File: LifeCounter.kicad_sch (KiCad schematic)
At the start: 17 parts, among them IC1 STM32H562RGT6, IC2 AP3012KTR-E1, J1 54104-4531

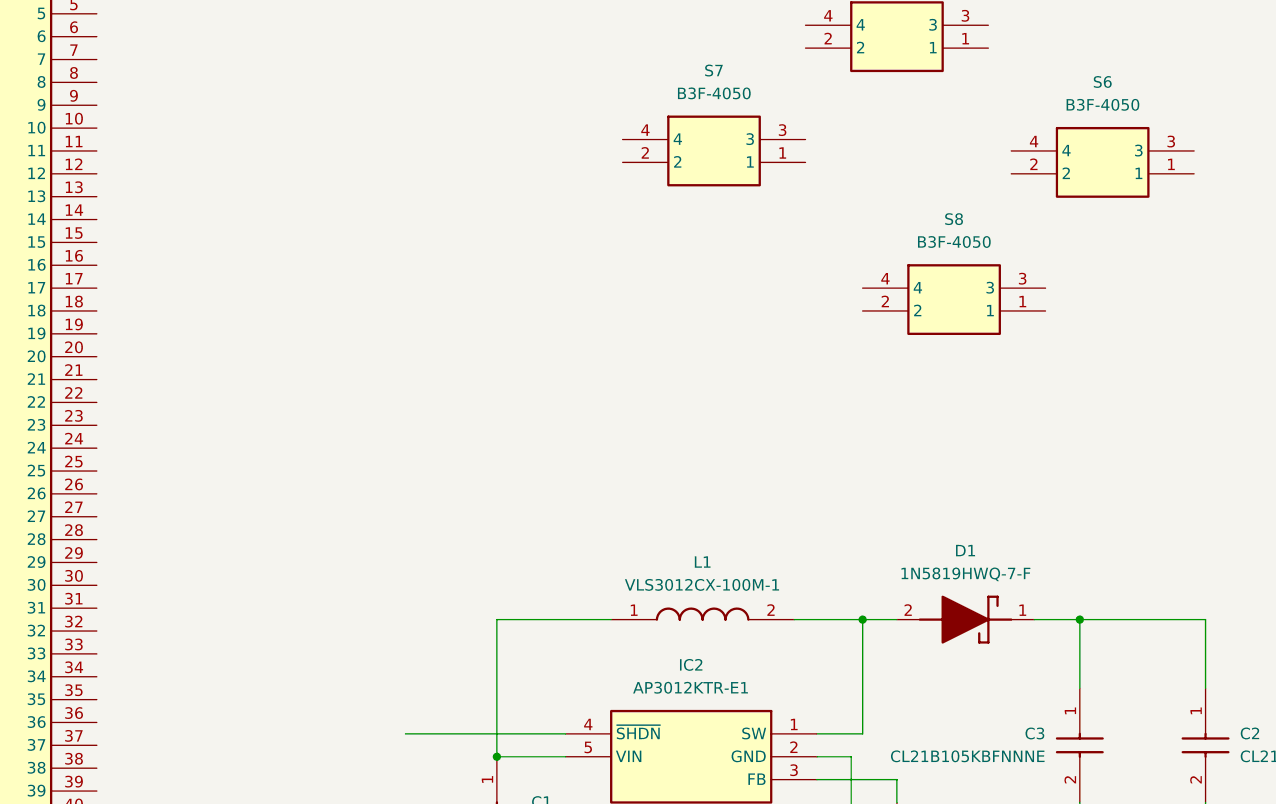
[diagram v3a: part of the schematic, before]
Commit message: bump version to v0.0.3, add USB C and TVS diode
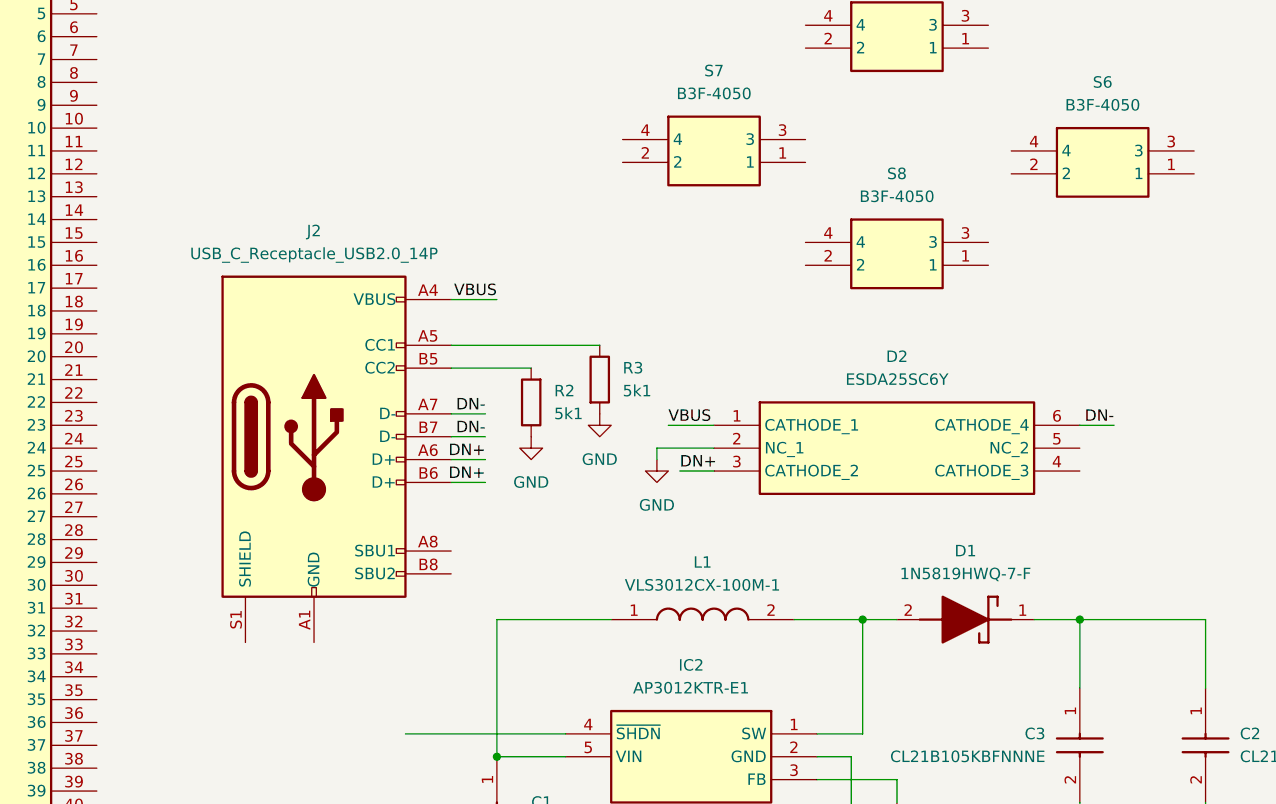
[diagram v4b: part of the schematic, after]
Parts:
- added D2: ESDA25SC6Y, LifeCounter-Footprints:STMicroelectronics_SOT95P280X145-6M, symbol LifeCounter-Symbols:ESDA25SC6Y
- added J2: USB_C_Receptacle_USB2.0_14P, Connector_USB:USB_C_Receptacle_GCT_USB4105-xx-A_16P_TopMnt_Horizontal, symbol Connector:USB_C_Receptacle_USB2.0_16P
- added R2, R3: 5k1, Resistor_SMD:R_0603_1608Metric_Pad0.98x0.95mm_HandSolder, symbol Device:R
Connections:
- new net: J2.A1 (GND), J2.A12 (GND), J2.B1 (GND), J2.B12 (GND)
- new net: J2.A5 (CC1), R3.1
- new net: J2.B5 (CC2), R2.2
- new net DN+: D2.3 (CATHODE_2), J2.A6 (D+), J2.B6 (D+)
- new net DN-: D2.6 (CATHODE_4), J2.A7 (D-), J2.B7 (D-)
- new net GND: D2.2 (NC_1), R2.1, R3.2
- new net VBUS: D2.1 (CATHODE_1), J2.A4 (VBUS), J2.A9 (VBUS), J2.B4 (VBUS), J2.B9 (VBUS)
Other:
- moved on the sheet: S8

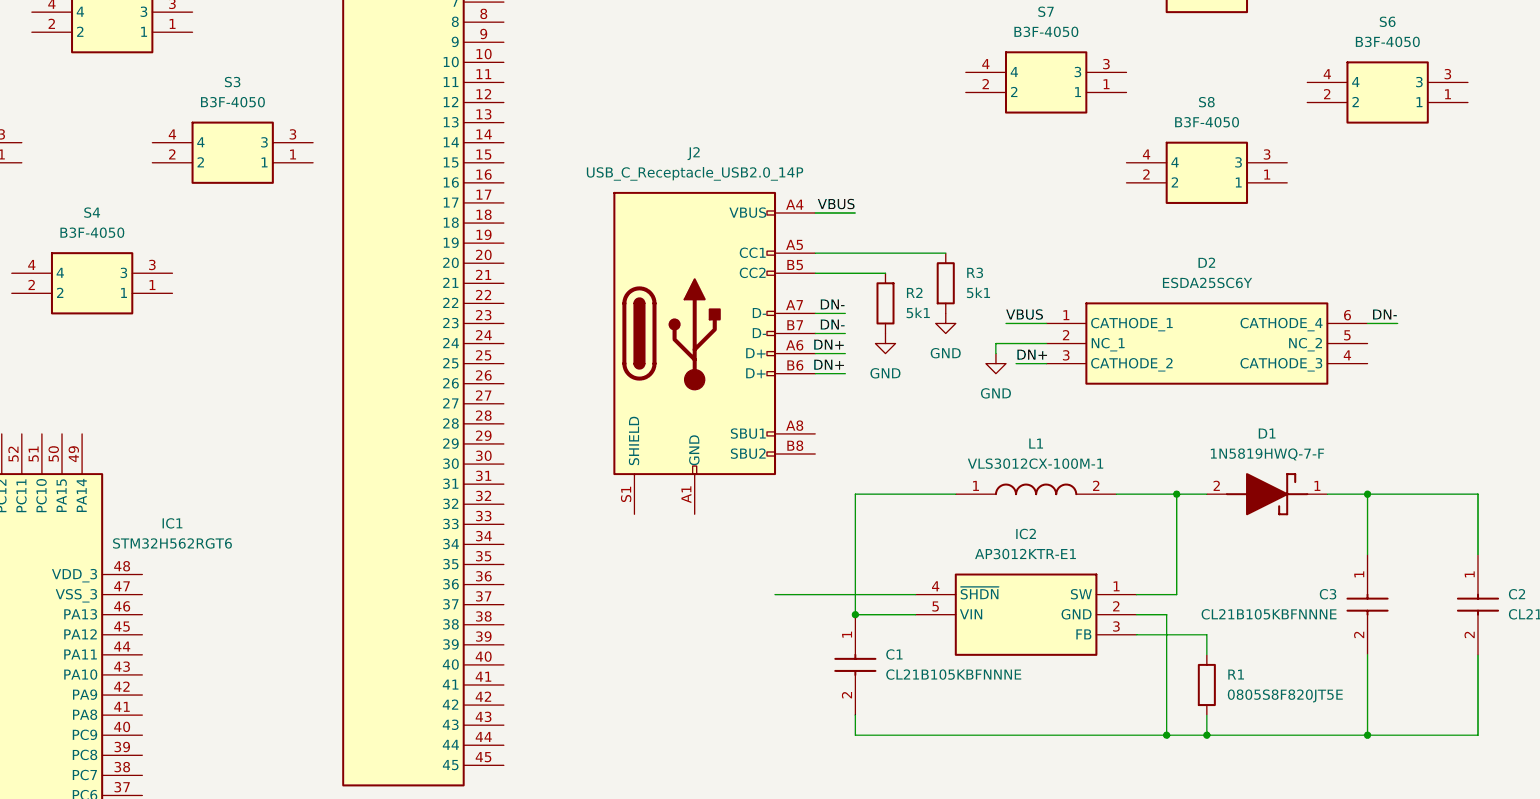
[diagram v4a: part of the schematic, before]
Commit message: added a 10uF 0603 capacitor for usb c VBUS
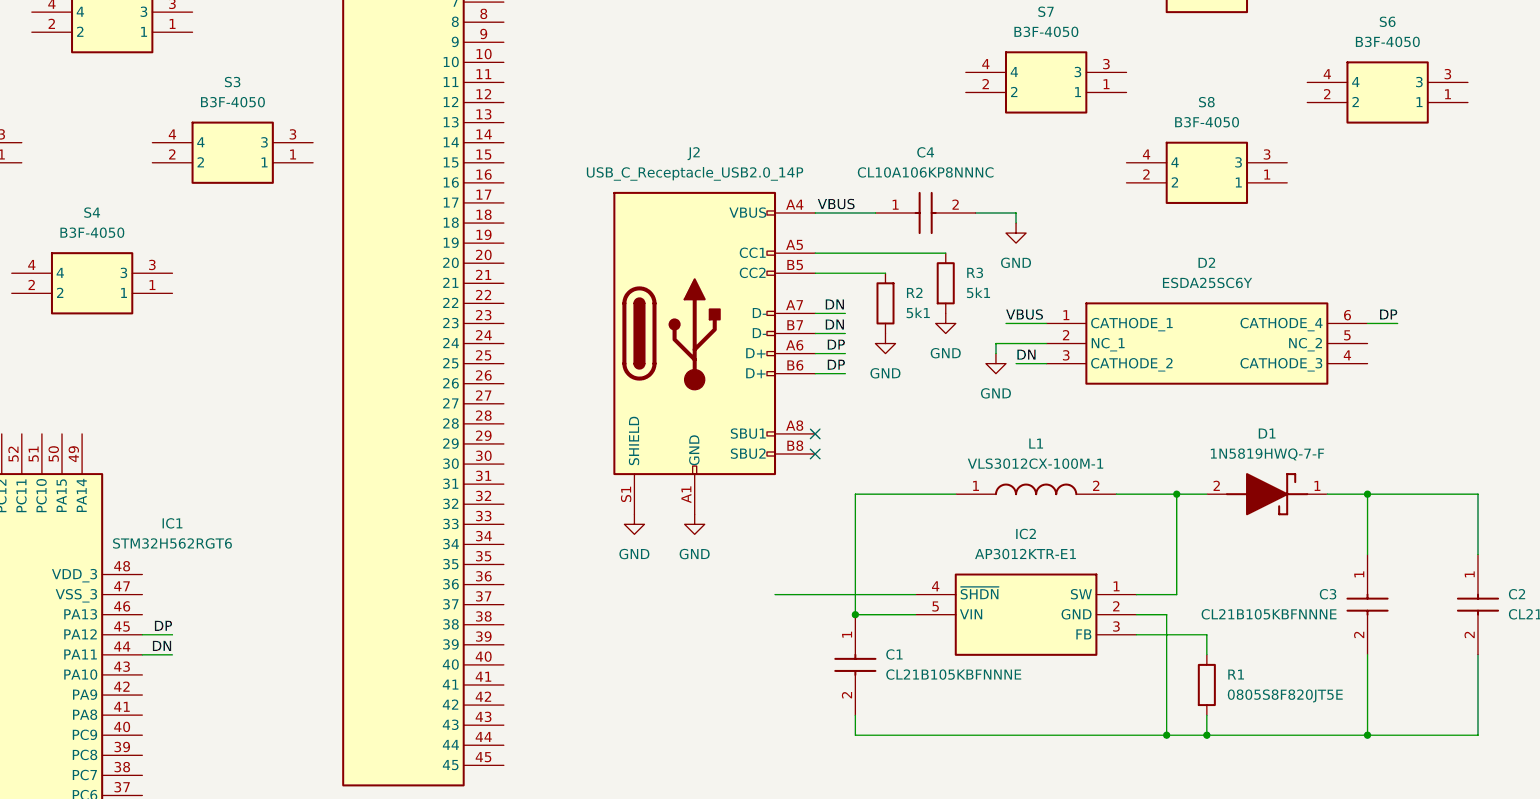
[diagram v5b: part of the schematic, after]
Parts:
- added C4: CL10A106KP8NNNC, LifeCounter-Footprints:Samsung_CAPC1608X90M, symbol LifeCounter-Symbols:CL10A106KP8NNNC
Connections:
- net GND: now also J2.A1 (GND), J2.A12 (GND), J2.B1 (GND), J2.B12 (GND), J2.S1 (SHIELD), C4.2
- net VBUS: now also C4.1
- net DN: now reaches IC1.44 (PA11)
- net DN: now also D2.3 (CATHODE_2), J2.A7 (D-), J2.B7 (D-)
- net DP: now reaches IC1.45 (PA12)
- net DP: now also D2.6 (CATHODE_4), J2.A6 (D+), J2.B6 (D+)
- removed net DN+: D2.3 (CATHODE_2), J2.A6 (D+), J2.B6 (D+)
- removed net DN-: D2.6 (CATHODE_4), J2.A7 (D-), J2.B7 (D-)
- no-connect marks 0 -> 2

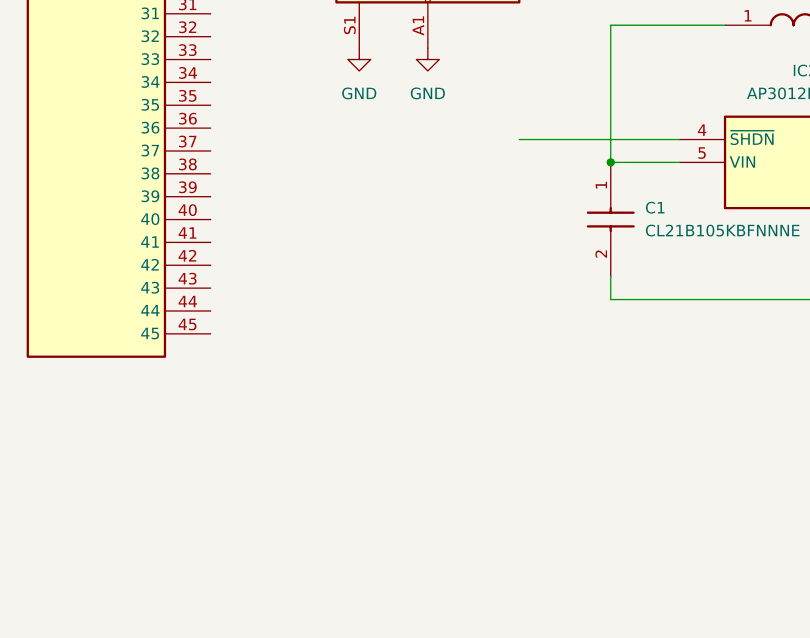
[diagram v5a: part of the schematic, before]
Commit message: added lipo charger and red led indicator diode
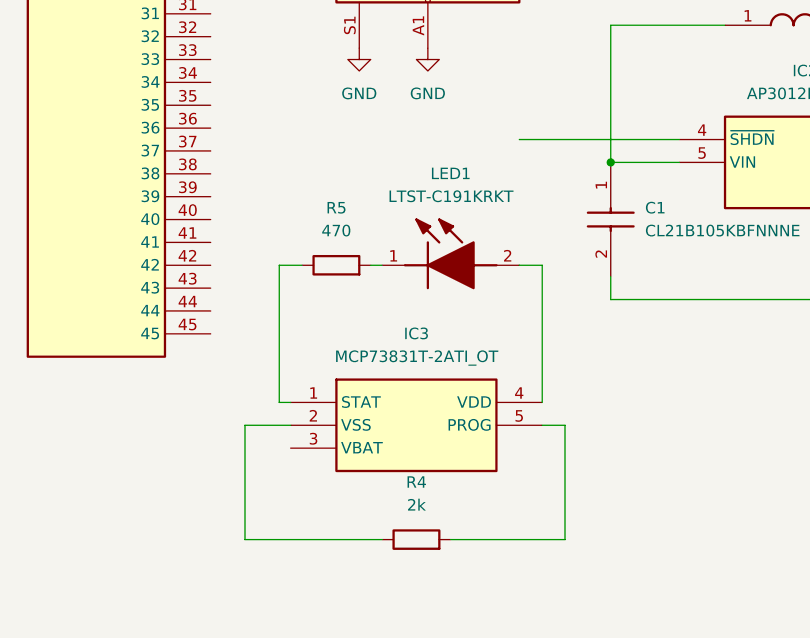
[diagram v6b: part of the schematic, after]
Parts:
- added IC3: MCP73831T-2ATI_OT, LifeCounter-Footprints:Microchip_SOT95P270X145-5M, symbol LifeCounter-Symbols:MCP73831T-2ATI_OT
- added LED1: LTST-C191KRKT, LifeCounter-Footprints:Liteon_LEDC1608X55M, symbol LifeCounter-Symbols:LTST-C191KRKT
- added R4: 2k, Resistor_SMD:R_0603_1608Metric_Pad0.98x0.95mm_HandSolder, symbol Device:R
- added R5: 470, Resistor_SMD:R_0603_1608Metric_Pad0.98x0.95mm_HandSolder, symbol Device:R
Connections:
- new net: IC3.1 (STAT), R5.1
- new net: LED1.1 (K), R5.2
- new net: IC3.2 (VSS), R4.1
- new net: IC3.5 (PROG), R4.2
- new net: IC3.4 (VDD), LED1.2 (A)

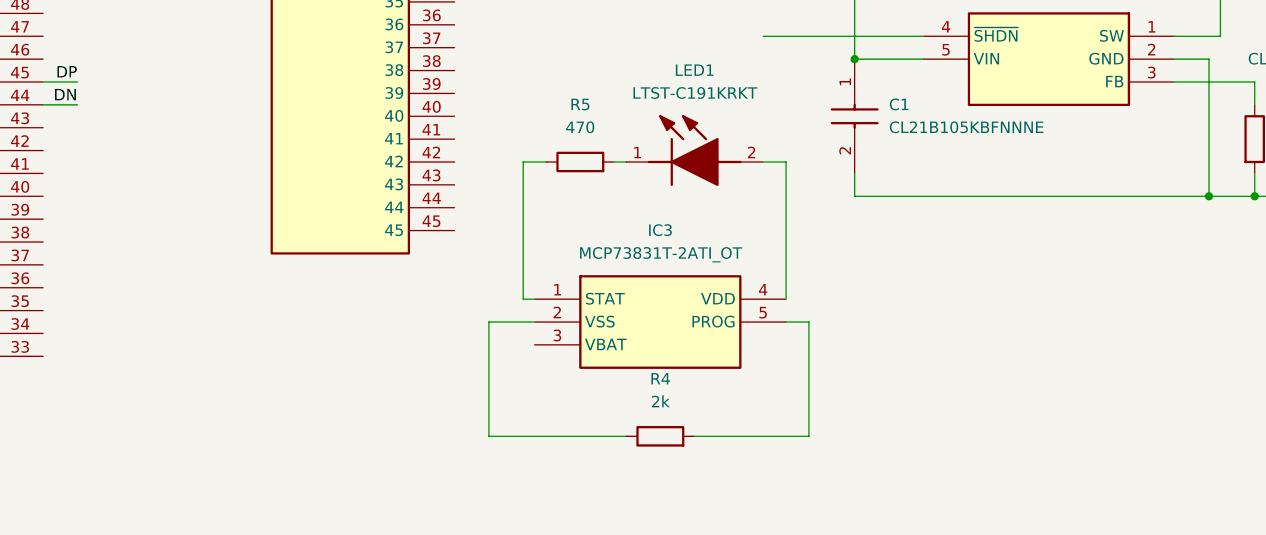
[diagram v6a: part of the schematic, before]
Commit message: added 4.7uF capacitors for the lipo charger
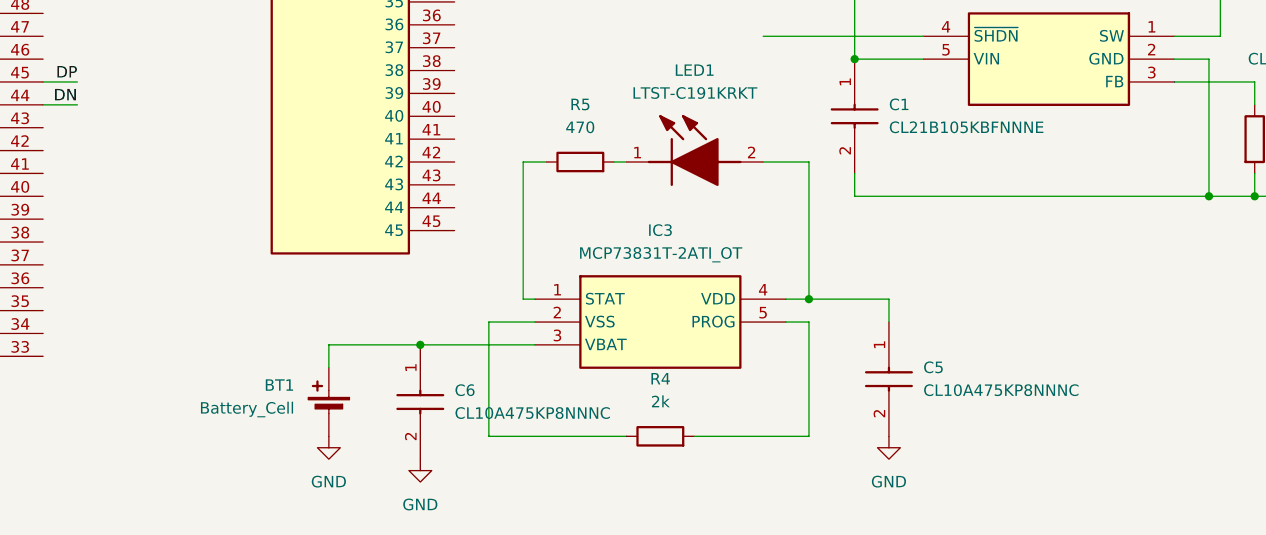
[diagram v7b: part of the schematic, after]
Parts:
- added BT1: Battery_Cell, symbol Device:Battery_Cell
- added C5, C6: CL10A475KP8NNNC, LifeCounter-Footprints:Samsung_CAPC1608X90M, symbol LifeCounter-Symbols:CL10A475KP8NNNC
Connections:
- net GND: now also BT1.2 (-), C5.2, C6.2
- net at IC3.3 (VBAT): now also BT1.1 (+), C6.1
- net at IC3.4 (VDD), LED1.2 (A): now also C5.1
